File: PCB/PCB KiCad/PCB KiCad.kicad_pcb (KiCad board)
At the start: 2 copper layers, 80 x 120 mm, 73 parts, among them J1 ADC Debug, J2 LED Debug, J3 Qwiic, SW1 MCU_RESET, SW2 TRIGGER, U1 OPA2376xxD, U2 ADS1256IDBT, U3 LM285D-2.5, U4 AMS1117-3.3, U5 TLC59208FIPWR, Y1 7.68MHz

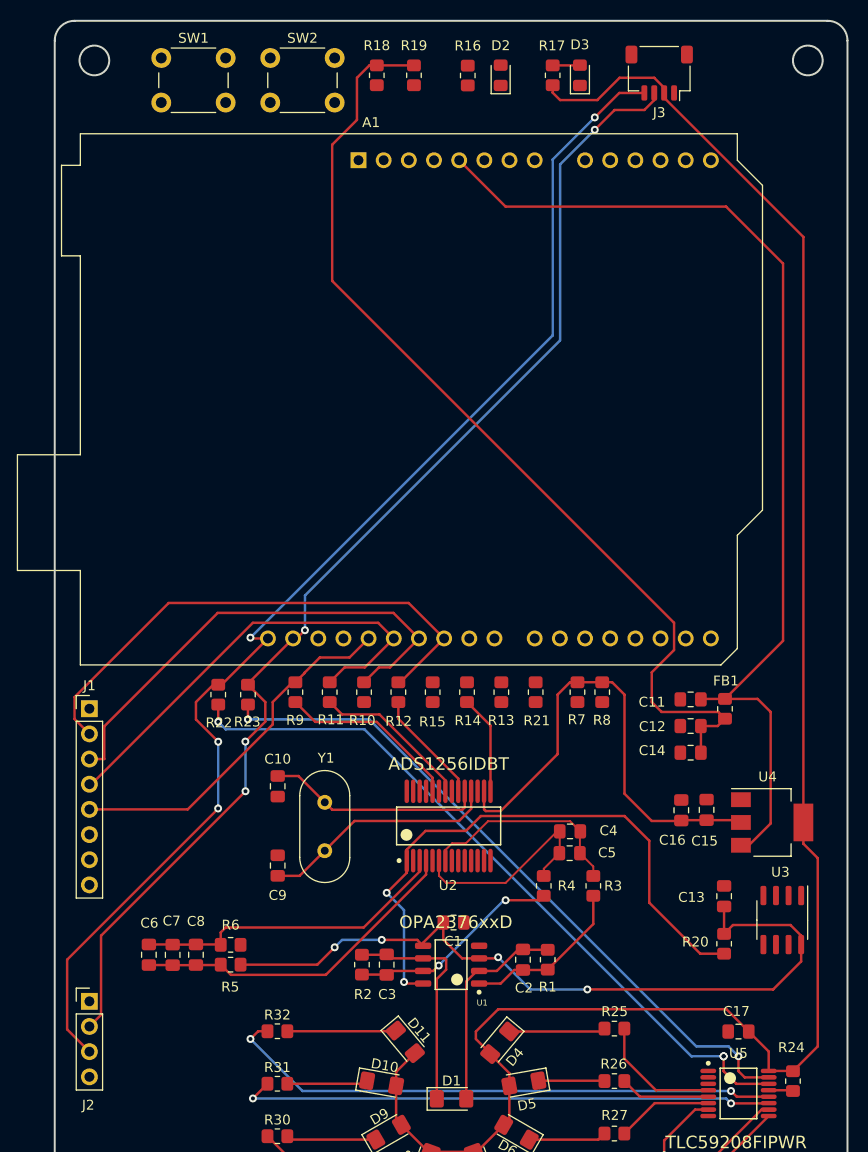
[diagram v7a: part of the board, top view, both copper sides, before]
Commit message: routing: swap order of J1 ADC signals, swap buttons order
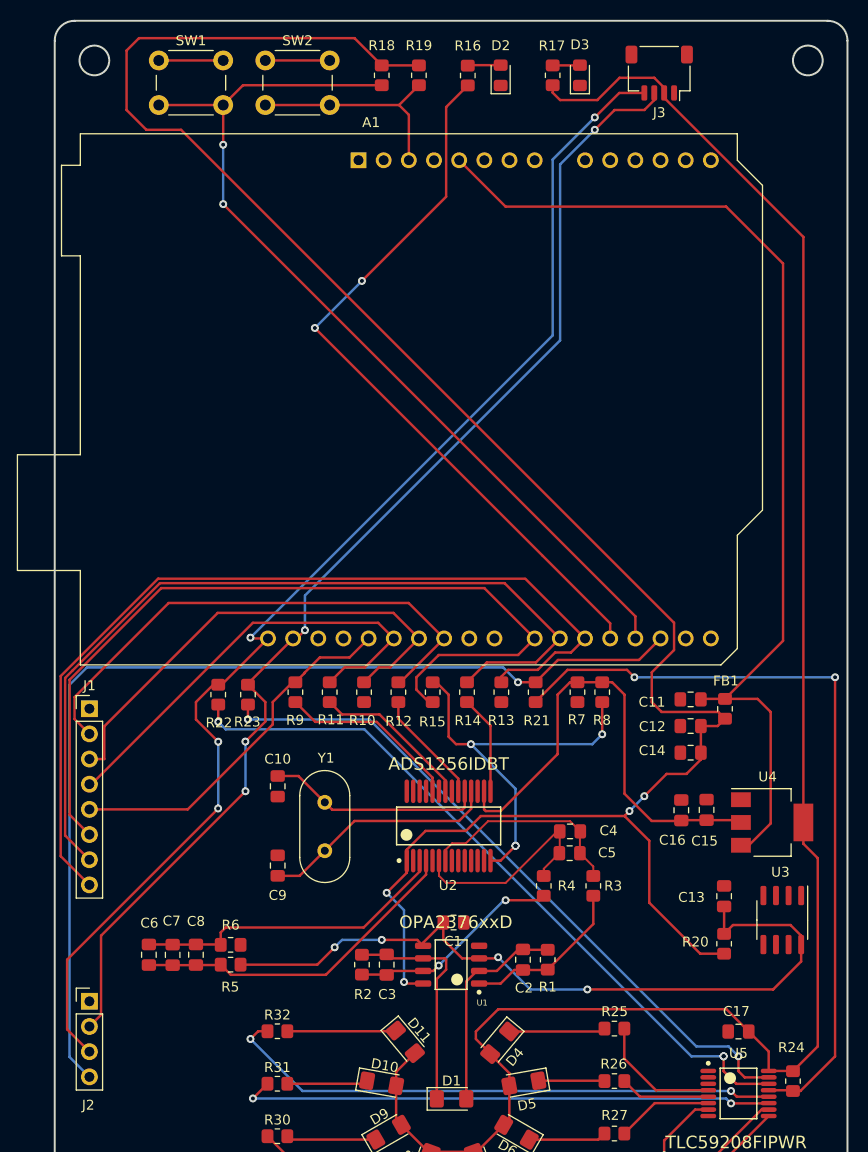
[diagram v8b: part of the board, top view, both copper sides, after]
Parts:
- moved SW1 11.3 mm to (53.5, 32.0)
- moved SW2 10.5 mm to (64.2, 32.0)
- moved R19 4.25 mm to (79.8, 33.5)
- moved R18 3.25 mm to (76.0, 33.5)
- renumbered R19 to R18, R18 to R19, SW2 to SW1, SW1 to SW2
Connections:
- J1 pad 6: /ADC/ADC DRDY -> /ADC/ADC PDWN
- J1 pad 8: /ADC/ADC PDWN -> /ADC/ADC DRDY
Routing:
- net /LED/LED RESET: track 0.00 -> 103.2 mm, vias 0 -> 1
- net /MCU + IO/TRIGGER: track 0.00 -> 94.4 mm, vias 0 -> 2
- net /ADC/ADC DRDY: track 0.00 -> 92.3 mm
- net /ADC/ADC RESET: track 0.00 -> 86.8 mm
- net /ADC/ADC PDWN: track 0.00 -> 86.3 mm
- net Net-(R21-Pad2): track 2.48 -> 78.3 mm, vias 0 -> 2
- net /MCU + IO/LED BLUE: track 0.00 -> 75.2 mm, vias 0 -> 2
- net +5V: track 158.8 -> 206.8 mm, vias 2 -> 4
- net Net-(R15-Pad2): track 0.00 -> 41.1 mm, vias 0 -> 4
- net /MCU + IO/MCU RESET: track 0.00 -> 22.3 mm
- net GND: track 0.00 -> 13.0 mm
- net Net-(D2-Pad2): track 0.00 -> 3.34 mm
